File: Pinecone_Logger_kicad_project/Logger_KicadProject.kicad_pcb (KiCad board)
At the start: 2 copper layers, 45 parts, among them J1 PwrJack-RESCUE-Logger_KicadPr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, J2 Cortex_Debug_Connector_(10_pi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, J3 SD_Micro_Slot, J4 9_pin_sdi_terminal, J5 6_pin_dht_term, J6 6_pin_Dend_term, J7 10_pin_tc_term, Q1 AO3420, Q2 AO3420, Q3 AO3420, Q4 AO3420, U2 MIC5211_Dual_Regulator, U3 AP2281, U4 DS1302, U5 MAX4618, U6 MAX31856, Y1 32.768kHz

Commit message: pcb partially done, pushing to work remotely
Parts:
- added J8: OSTVN10A150, Lubrecht_Pcb_footprints:10_pin_2.54mm_term, F.Cu at (14.8, 16.2)
- added U1: SAMD20G17A-A, Housings_QFP:TQFP-48_7x7mm_Pitch0.5mm, F.Cu at (46.2, 44.2)
- C1, C6: value 10uF -> GRM219R61A106KE44D
- C10, C3: value 1uF -> GRM21BR71C105KA01L
- C11, C12, C13, C14, C15, C16, C17, C18, C2, C4, C5, C7, C8, C9: value .1uF -> CC0603ZRY5V9BB104
- J1: value PwrJack-RESCUE-Logger_KicadProject -> PJ-102A
- J2: value Cortex_Debug_Connector_(10_pin) -> M50-3600542
- J3: value SD_Micro_Slot -> DM3AT-SF-PEJM5
- J4: value 9_pin_sdi_terminal -> OSTVN06A150; footprint Lubrecht_Pcb_footprints:9_pin_sdi_terminal -> Lubrecht_Pcb_footprints:6_pin_2.54mm_term
- J5: value 6_pin_dht_term -> OSTVN06A150; footprint Lubrecht_Pcb_footprints:6_pin_junction_term -> Lubrecht_Pcb_footprints:6_pin_2.54mm_term
- J6: value 6_pin_Dend_term -> OSTVN06A150; footprint Lubrecht_Pcb_footprints:6_pin_junction_term -> Lubrecht_Pcb_footprints:6_pin_2.54mm_term
- J7: value 10_pin_tc_term -> OSTVN06A150; footprint Lubrecht_Pcb_footprints:10_pin_junction_term -> Lubrecht_Pcb_footprints:6_pin_2.54mm_term
- L1: value 10uH -> Z0805C221APMST
- R1, R3, R4, R5, R6, R7, R8: value 10K -> RC0805JR-0710KL
- R2: value 1K -> RC0805JR-071KL
- U2: value MIC5211_Dual_Regulator -> MIC5211
- U6: footprint Lubrecht_Pcb_footprints:TSSOP14 -> Housings_SSOP:TSSOP-14_4.4x5mm_Pitch0.65mm
- moved Y1 224.7 mm to (14.0, 52.0), turned to 270 degrees
- moved U4 219.0 mm to (17.8, 51.2)
- moved J5 201.5 mm to (48.8, 16.2)
- moved J6 191.2 mm to (14.2, 66.4)
- moved R3 188.0 mm to (-8.00, 61.0)
- moved C15 181.8 mm to (-20.5, 38.0)
- moved BT1 180.3 mm to (32.0, 42.4), turned to 180 degrees
- moved C16 177.3 mm to (-13.5, 33.0)
- moved C17 175.7 mm to (-13.5, 37.0)
- moved C14 174.2 mm to (-13.5, 41.0)
- moved C13 173.9 mm to (-14.5, 44.5)
- moved C11 173.0 mm to (-16.0, 51.5)
- moved C10 172.7 mm to (-17.0, 55.5)
- moved J3 170.0 mm to (60.0, 40.0)
- moved U5 169.6 mm to (31.4, 25.0)
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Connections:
- J5 pad 1: SWITCHED_5v -> SWITCHED_3v3
- J5 pad 2: SWITCHED_5v -> SWITCHED_3v3
- J5 pad 3: Net-(J5-Pad3) -> Dend1
- J5 pad 4: Net-(J5-Pad4) -> Dend2
- J6 pad 1: SWITCHED_3v3 -> SWITCHED_5v
- J6 pad 2: SWITCHED_3v3 -> Net-(J6-Pad2)
- J6 pad 3: Dend1 -> GND
- J6 pad 4: Dend2 -> SWITCHED_5v
- J6 pad 5: GND -> Net-(J6-Pad2)
- J7 pad 1: +12V -> SWITCHED_5v
- J7 pad 2: HEATER_SWITCHED_GND -> Net-(J6-Pad2)
- J7 pad 3: Net-(J7-Pad3) -> GND
- J7 pad 4: Net-(J7-Pad4) -> SWITCHED_5v
- J7 pad 5: Net-(J7-Pad5) -> Net-(J6-Pad2)
- J7 pad 6: Net-(J7-Pad6) -> GND
- Q2 pad 3: Net-(J4-Pad4) -> Net-(J6-Pad2)
- Q3 pad 3: Net-(J5-Pad3) -> Net-(J4-Pad3)
- Q4 pad 3: Net-(J5-Pad4) -> Net-(J4-Pad4)
- R3 pad 2: Net-(J4-Pad4) -> Net-(J6-Pad2)
- R5 pad 2: Net-(J5-Pad3) -> Net-(J4-Pad3)
- R6 pad 2: Net-(J5-Pad4) -> Net-(J4-Pad4)
- U5 pad 1: Net-(J7-Pad3) -> Net-(J8-Pad3)
- U5 pad 11: Net-(J7-Pad10) -> Net-(J8-Pad10)
- U5 pad 12: Net-(J7-Pad7) -> Net-(J8-Pad7)
- U5 pad 13: Net-(J7-Pad8) -> Net-(J8-Pad8)
- U5 pad 15: Net-(J7-Pad9) -> Net-(J8-Pad9)
- U5 pad 2: Net-(J7-Pad5) -> Net-(J8-Pad5)
- U5 pad 4: Net-(J7-Pad6) -> Net-(J8-Pad6)
- U5 pad 5: Net-(J7-Pad4) -> Net-(J8-Pad4)
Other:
- copper layers 2 -> 4
- net class large added: clearance 0.2, trace_width 0.5, via_dia 0.6, via_drill 0.4

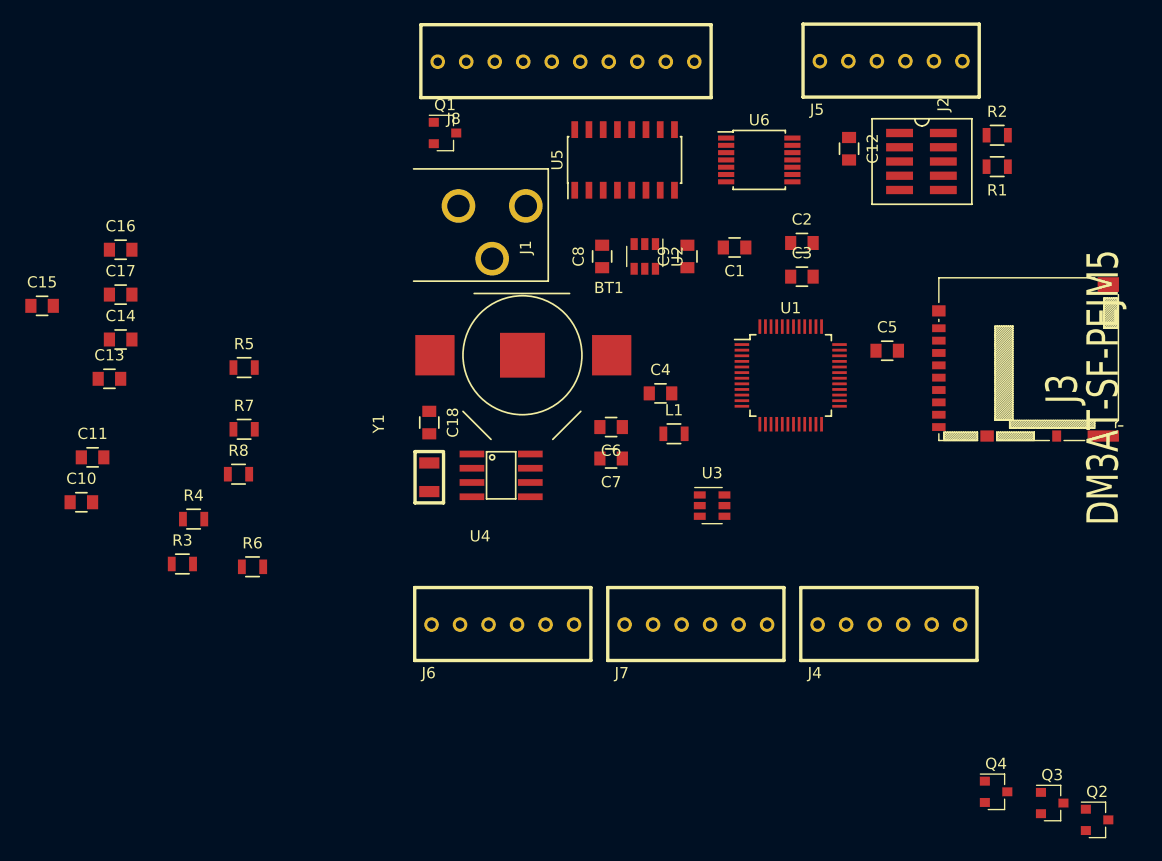
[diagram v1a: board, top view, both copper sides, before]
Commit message: finished circuit design, firmware needs updating to respect pin changes
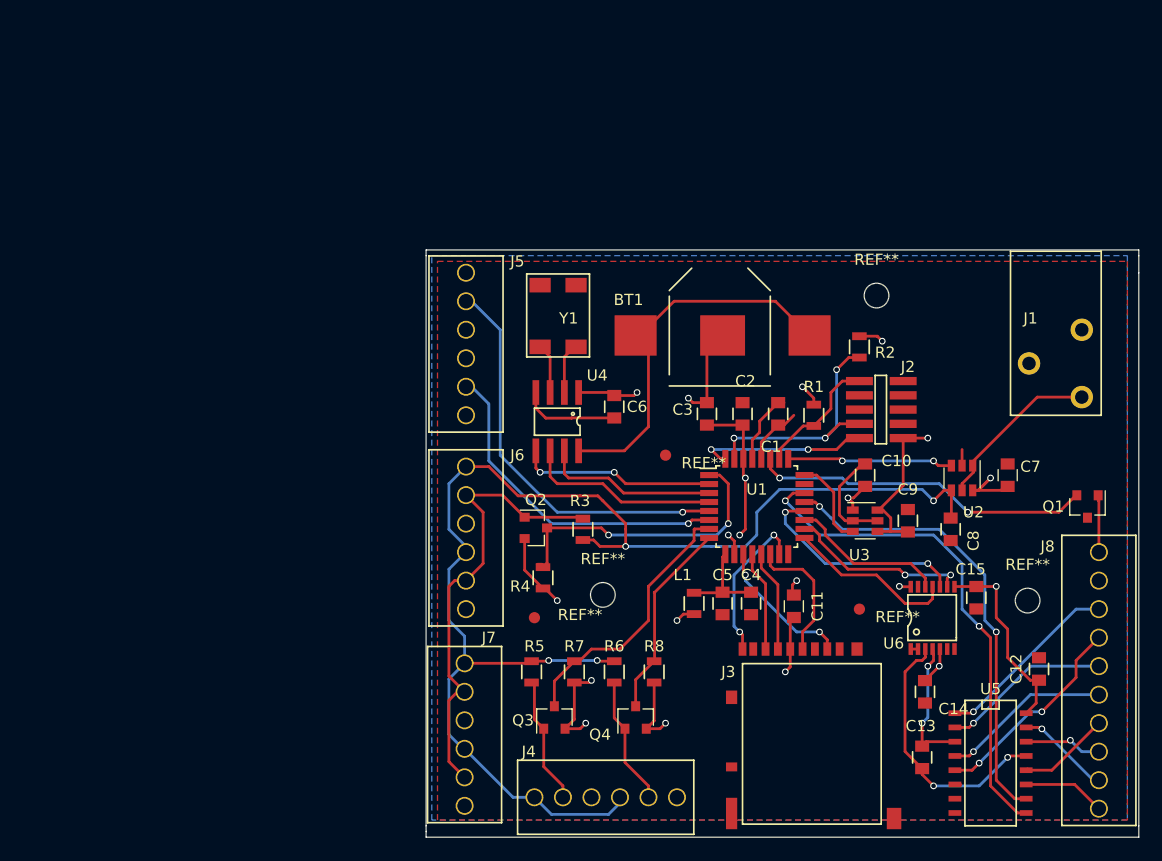
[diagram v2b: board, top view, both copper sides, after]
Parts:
- removed C16, C17, C18: CC0603ZRY5V9BB104, Capacitors_SMD:C_0805
- added REF**: MountingHole_2.2mm_M2, Mounting_Holes:MountingHole_2.2mm_M2, F.Cu at (67.3, 64.3)
- added REF**: MountingHole_2.2mm_M2, Mounting_Holes:MountingHole_2.2mm_M2, F.Cu at (29.5, 63.8)
- added REF**: MountingHole_2.2mm_M2, Mounting_Holes:MountingHole_2.2mm_M2, F.Cu at (53.8, 37.1)
- added REF**: Fiducial_1mm_Dia_2.54mm_Outer_CopperTop, Fiducials:Fiducial_1mm_Dia_2.54mm_Outer_CopperTop, F.Cu at (23.4, 65.8)
- added REF**: Fiducial_1mm_Dia_2.54mm_Outer_CopperTop, Fiducials:Fiducial_1mm_Dia_2.54mm_Outer_CopperTop, F.Cu at (35.1, 51.3)
- added REF**: Fiducial_1mm_Dia_2.54mm_Outer_CopperTop, Fiducials:Fiducial_1mm_Dia_2.54mm_Outer_CopperTop, F.Cu at (52.3, 65.0)
- BT1: footprint Lubrecht_Pcb_footprints:S8201_Bat_Holder -> Pinecone_footprints:S8201R_Batt_Holder
- C1: value GRM219R61A106KE44D -> GRM21BR71C105KA01L
- C10: value GRM21BR71C105KA01L -> CC0603ZRY5V9BB104
- C3: value GRM21BR71C105KA01L -> GRM219R61A106KE44D
- C4: value CC0603ZRY5V9BB104 -> GRM219R61A106KE44D
- C6: value GRM219R61A106KE44D -> CC0603ZRY5V9BB104
- C9: value CC0603ZRY5V9BB104 -> GRM21BR71C105KA01L
- J1: footprint Lubrecht_Pcb_footprints:PJ-102a -> Pinecone_footprints:PJ-102A
- J2: footprint SWD_Connector_SMD -> Pinecone_footprints:10_Pin_Cortex_SMD
- J3: footprint Lubrecht_Pcb_footprints:hirose-dm3at -> Pinecone_footprints:Hirose_DM3AT
- J4, J5, J6, J7: footprint Lubrecht_Pcb_footprints:6_pin_2.54mm_term -> Pinecone_footprints:OSTVN06A150_6_Pin_Terminal
- J8: value OSTVN10A150 -> 10_Pin_Header; footprint Lubrecht_Pcb_footprints:10_pin_2.54mm_term -> Pinecone_footprints:OSTVN10A150_10_pin_term
- U1: value SAMD20G17A-A -> SAMD20E16A-A; footprint Housings_QFP:TQFP-48_7x7mm_Pitch0.5mm -> Housings_QFP:TQFP-32_7x7mm_Pitch0.8mm
- U4: footprint Lubrecht_Pcb_footprints:SOIC-8 -> Pinecone_footprints:SOIC-8
- U5: footprint Housings_SOIC:SOIC-16_3.9x9.9mm_Pitch1.27mm -> SMD_Packages:SO-16-N
- U6: footprint Housings_SSOP:TSSOP-14_4.4x5mm_Pitch0.65mm -> Pinecone_footprints:TSSOP-14
- Y1: value 32.768kHz -> MC-306_32.768K-E3; footprint Lubrecht_Pcb_footprints:MC-306_Xtal -> Pinecone_footprints:MC-306_32.768K-E3
- moved C15 87.2 mm to (62.7, 64.0), turned to 270 degrees
- moved C13 79.9 mm to (57.9, 78.2), turned to 270 degrees
- moved C14 78.2 mm to (58.2, 72.4), turned to 270 degrees
- moved J8 73.3 mm to (73.7, 59.9), turned to 270 degrees
- moved C10 69.9 mm to (52.8, 53.1), turned to 90 degrees
- moved Q1 66.2 mm to (72.6, 55.9), turned to 270 degrees
- moved C11 63.9 mm to (46.5, 64.8), turned to 270 degrees
- moved U5 62.9 mm to (64.0, 78.7), turned to 270 degrees
- moved Q2 56.4 mm to (23.5, 57.8)
- moved J1 52.9 mm to (72.1, 40.1), turned to 0 degrees
- moved C12 49.4 mm to (68.3, 70.4), turned to 90 degrees
- moved U6 45.6 mm to (56.9, 68.6), turned to 90 degrees
- moved Q3 45.0 mm to (25.1, 74.7), turned to 90 degrees
- moved R8 41.0 mm to (34.0, 70.6), turned to 90 degrees
- moved C8 39.4 mm to (60.5, 57.9), turned to 270 degrees
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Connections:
- C1 pad 1: GND -> Net-(C1-Pad1)
- C1 pad 2: +3V3 -> GND
- C10 pad 1: +3V3 -> SWITCHED_3v3
- C11 pad 1: SWITCHED_3v3 -> GND
- C11 pad 2: GND -> SWITCHED_3v3
- C12 pad 1: +3V3 -> SWITCHED_3v3
- C13 pad 1: SWITCHED_3v3 -> Net-(C13-Pad1)
- C13 pad 2: GND -> Net-(C13-Pad2)
- C15 pad 1: Net-(C15-Pad1) -> SWITCHED_3v3
- C15 pad 2: Net-(C15-Pad2) -> GND
- C3 pad 1: Net-(C3-Pad1) -> +3V3
- C4 pad 1: +3V3 -> GND
- C4 pad 2: GND -> Net-(C4-Pad2)
- C5 pad 1: +3V3 -> GND
- C5 pad 2: GND -> Net-(C4-Pad2)
- C6 pad 1: Net-(C6-Pad1) -> +3V3
- C7 pad 1: Net-(C6-Pad1) -> +3V3
- J3 pad 10: Net-(J3-Pad10) -> (no net)
- J3 pad 9: Net-(J3-Pad9) -> (no net)
- J4 pad 2: SWITCHED_5v -> Net-(J4-Pad2)
- J4 pad 3: Net-(J4-Pad3) -> GND
- J4 pad 4: Net-(J4-Pad4) -> SWITCHED_5v
- J4 pad 5: GND -> Net-(J4-Pad5)
- J5 pad 2: SWITCHED_3v3 -> Dend1
- J5 pad 3: Dend1 -> GND
- J5 pad 4: Dend2 -> SWITCHED_3v3
- J5 pad 5: GND -> Dend2
- J8 pad 1: +12V -> HEATER_SWITCHED_GND
- J8 pad 2: HEATER_SWITCHED_GND -> +12V
- L1 pad 1: +3V3 -> Net-(C4-Pad2)
- L1 pad 2: Net-(C6-Pad1) -> +3V3
- Q1 pad 1: HEATER_ENABLE -> HEATER_SWITCHED_GND
- Q1 pad 2: GND -> HEATER_ENABLE
- Q1 pad 3: HEATER_SWITCHED_GND -> GND
- Q2 pad 1: SWITCHED_3v3 -> Net-(J6-Pad2)
- Q2 pad 2: SDI_3v3_DATA -> SWITCHED_3v3
- Q2 pad 3: Net-(J6-Pad2) -> SDI_3v3_DATA
- Q3 pad 1: SWITCHED_3v3 -> Net-(J4-Pad2)
- Q3 pad 2: DHT22_1 -> SWITCHED_3v3
- Q3 pad 3: Net-(J4-Pad3) -> DHT22_1
- Q4 pad 1: SWITCHED_3v3 -> Net-(J4-Pad5)
- Q4 pad 2: DHT22_2 -> SWITCHED_3v3
- Q4 pad 3: Net-(J4-Pad4) -> DHT22_2
- R2 pad 1: SWDCLK -> +3V3
- R2 pad 2: +3V3 -> SWDCLK
- R5 pad 2: Net-(J4-Pad3) -> Net-(J4-Pad2)
- R6 pad 2: Net-(J4-Pad4) -> Net-(J4-Pad5)
- U1 pad 1: DHT22_1 -> SDI_3v3_DATA
- U1 pad 10: SD_SERCOM_PAD1_CS -> GND
- U1 pad 11: SD_SERCOM_PAD2_MOSI -> SD_SERCOM_PAD0_MISO
- U1 pad 12: SD_SERCOM_PAD3_SCK -> SD_SERCOM_PAD1_CS
- U1 pad 13: Net-(U1-Pad13) -> SD_SERCOM_PAD2_MOSI
- U1 pad 14: DS1302_SCLK -> SD_SERCOM_PAD3_SCK
- U1 pad 15: DS1302_IO -> SD_CHIP_DETECT
- U1 pad 16: DS1302_CE -> Net-(U1-Pad16)
- U1 pad 17: +3V3 -> MAX31856_SERCOM_PAD0_MISO
- U1 pad 18: GND -> MAX31856_SERCOM_PAD1_CS
- U1 pad 19: 3v3_PWR_ENABLE -> MAX31856_SERCOM_PAD2_MOSI
- U1 pad 2: DHT22_2 -> DS1302_CE
- U1 pad 20: HEATER_ENABLE -> MAX31856_SERCOM_PAD3_SCK
- U1 pad 21: Net-(U1-Pad21) -> MUX_SEL_A
- U1 pad 22: Net-(U1-Pad22) -> MUX_SEL_B
- U1 pad 24: Net-(U1-Pad24) -> 3v3_PWR_ENABLE
- U1 pad 25: MAX31856_SERCOM_PAD0_MISO -> 5v_PWR_ENABLE
- U1 pad 26: MAX31856_SERCOM_PAD1_CS -> RESET
- U1 pad 27: MAX31856_SERCOM_PAD2_MOSI -> HEATER_ENABLE
- U1 pad 28: MAX31856_SERCOM_PAD3_SCK -> GND
- U1 pad 29: MUX_SEL_A -> Net-(C1-Pad1)
- U1 pad 3: Dend1 -> DS1302_SCLK
- U1 pad 30: MUX_SEL_B -> +3V3
- U1 pad 31: Net-(U1-Pad31) -> SWDCLK
- U1 pad 32: Net-(U1-Pad32) -> SWDIO
- U1 pad 4: Dend2 -> DS1302_IO
- U1 pad 5: GND -> Dend1
- U1 pad 6: Net-(C6-Pad1) -> Dend2
- U1 pad 7: Net-(U1-Pad7) -> DHT22_1
- U1 pad 8: SD_CHIP_DETECT -> DHT22_2
- U1 pad 9: SD_SERCOM_PAD0_MISO -> Net-(C4-Pad2)
- U5 pad 13: Net-(J8-Pad8) -> Net-(C13-Pad2)
- U5 pad 14: Net-(C15-Pad1) -> Net-(J8-Pad8)
- U5 pad 3: Net-(C15-Pad2) -> Net-(C13-Pad1)
- U6 pad 3: Net-(C15-Pad1) -> Net-(C13-Pad2)
- U6 pad 4: Net-(C15-Pad2) -> Net-(C13-Pad1)
- Y1 pad 1: Net-(U4-Pad2) -> Net-(U4-Pad3)
- Y1 pad 2: Net-(U4-Pad3) -> Net-(Y1-Pad2)
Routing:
- net SWITCHED_5v: track 0.00 -> 118.2 mm, vias 0 -> 4
- net SWITCHED_3v3: track 0.00 -> 50.1 mm, vias 0 -> 8
- net +3V3: track 0.00 -> 47.0 mm, vias 0 -> 8
- net MUX_SEL_B: track 0.00 -> 45.1 mm, vias 0 -> 2
- net MUX_SEL_A: track 0.00 -> 40.8 mm, vias 0 -> 2
- net Net-(J6-Pad2): track 0.00 -> 40.6 mm
- net GND: track 0.00 -> 39.3 mm, vias 0 -> 4
- net Dend1: track 0.00 -> 36.0 mm, vias 0 -> 1
- net Net-(BT1-Pad1): track 0.00 -> 34.3 mm
- net HEATER_ENABLE: track 0.00 -> 30.4 mm, vias 0 -> 2
- net Dend2: track 0.00 -> 29.8 mm, vias 0 -> 1
- net SDI_3v3_DATA: track 0.00 -> 26.5 mm, vias 0 -> 2
- net DHT22_1: track 0.00 -> 24.1 mm
- net Net-(C13-Pad2): track 0.00 -> 23.7 mm, vias 0 -> 2
- net SWDCLK: track 0.00 -> 22.6 mm, vias 0 -> 3
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- added copper zone on Vcc.Cu, net +12V
- added copper zone on Vcc.Cu, net +3V3
- added copper zone on B.Cu, net GND
- added copper zone on F.Cu, net GND
- added copper zone on Gnd.Cu, net GND
- added copper zone on Vcc.Cu, net SWITCHED_3v3
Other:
- board outline added: 63.5 x 52.3 mm
- net class large removed
- rule pad_to_mask_clearance: 0.2 -> 0
- board text added: "Design by Tim Anderson Univ. Montana"
- board text added: "J5, Dendro"

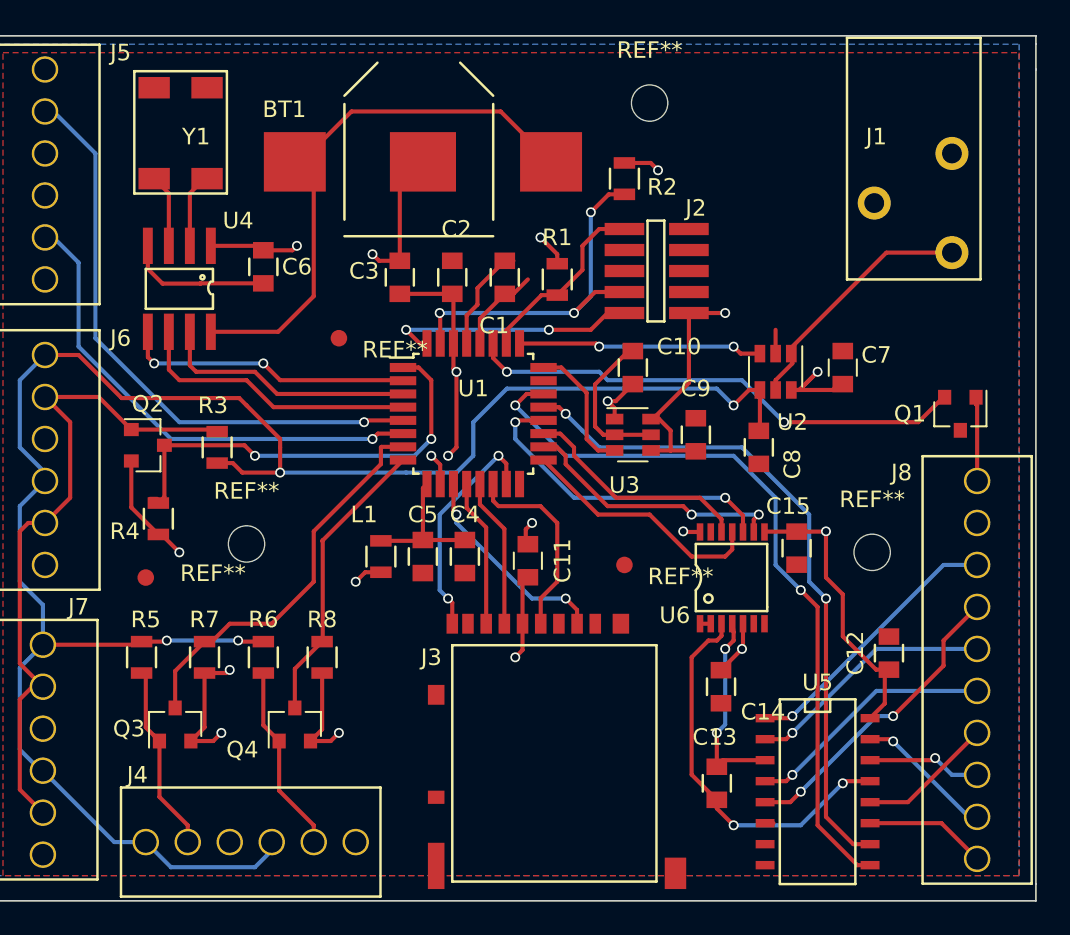
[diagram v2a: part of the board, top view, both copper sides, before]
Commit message: added .pretty footprint libraries to the repo
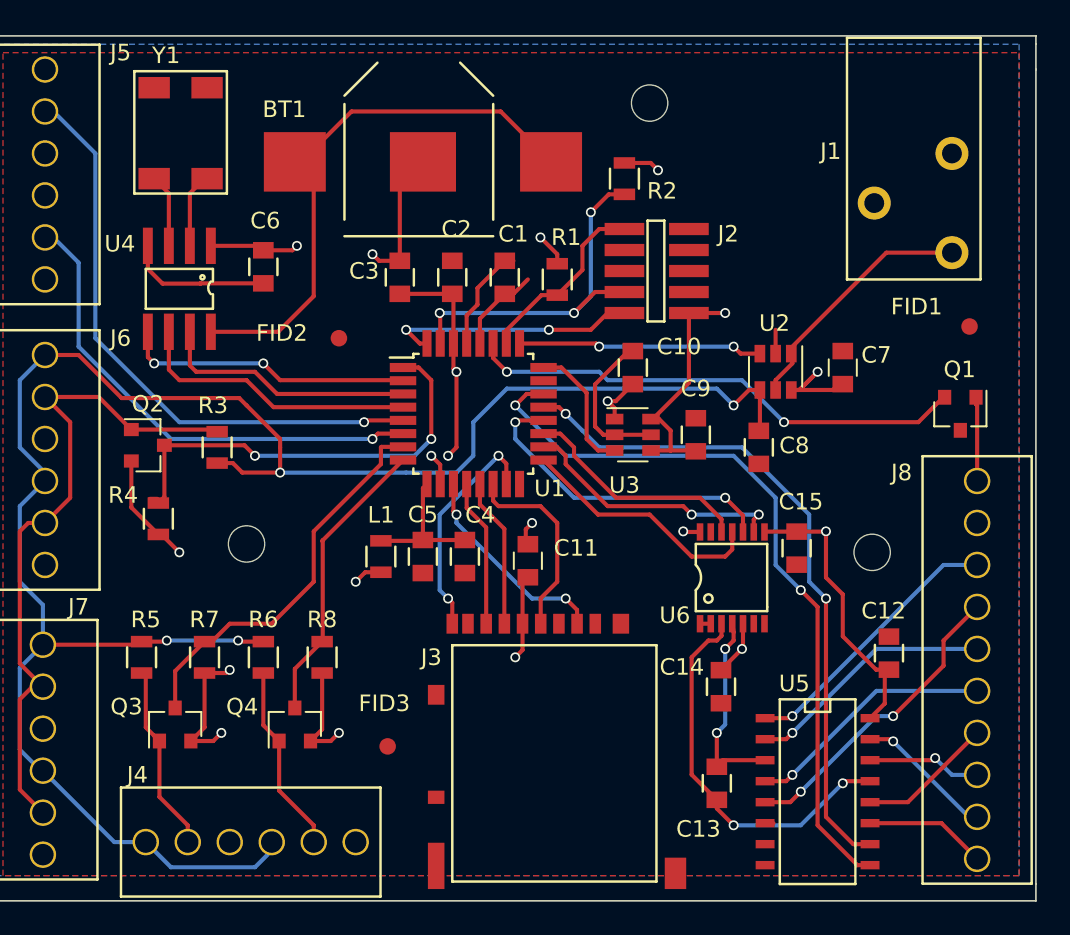
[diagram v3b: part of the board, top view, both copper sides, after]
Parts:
- moved FID1 25.4 mm to (73.2, 50.6)
- moved FID3 17.8 mm to (38.0, 76.0)
- renumbered REF** to FID1, REF** to FID2, REF** to FID3
